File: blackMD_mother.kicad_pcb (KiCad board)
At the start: 2 copper layers, 99.1 x 99.1 mm, 19 parts

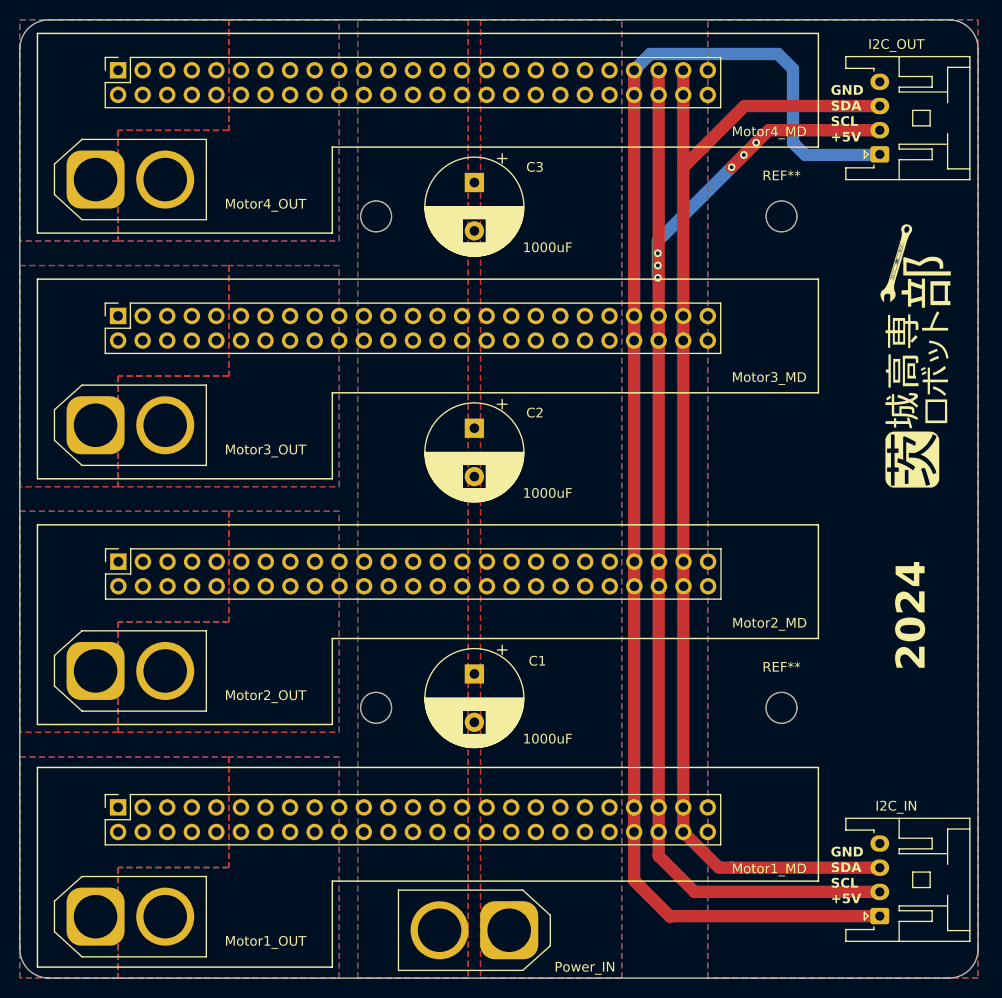
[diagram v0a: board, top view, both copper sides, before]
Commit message: swap MotorA & MotorB
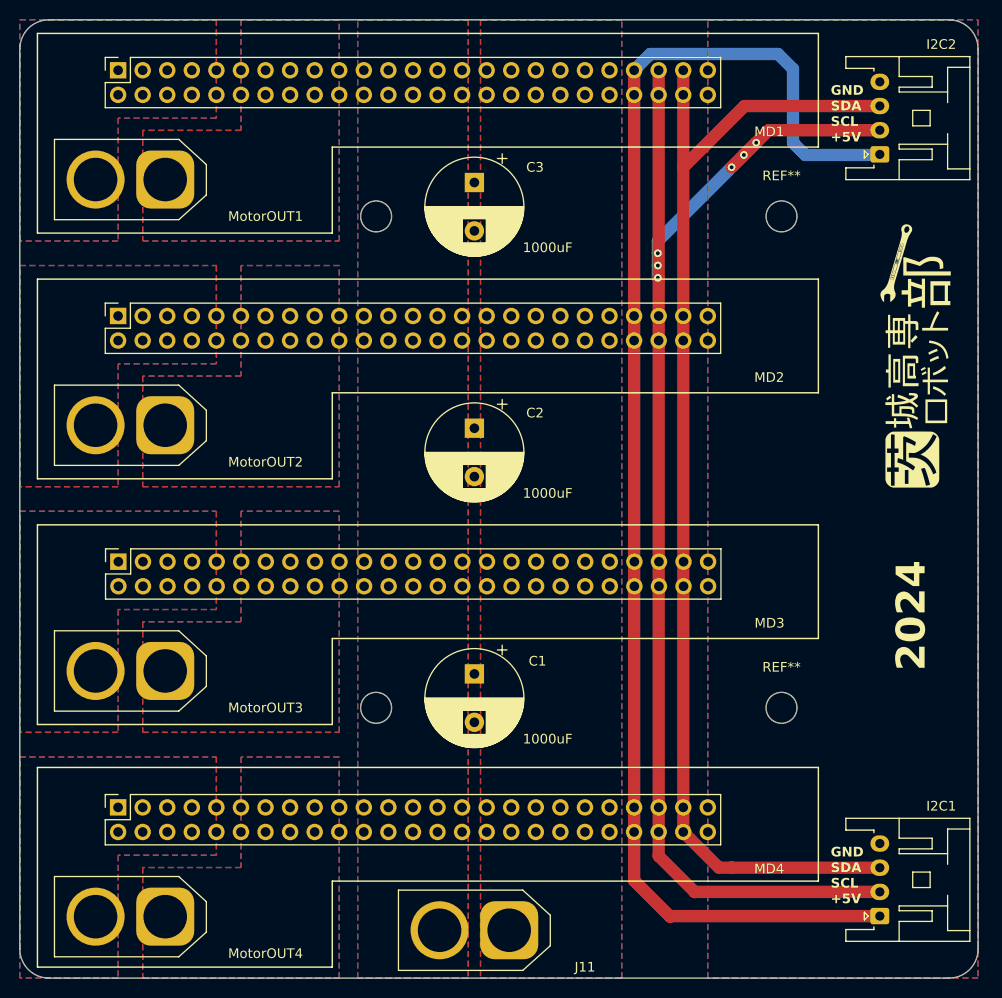
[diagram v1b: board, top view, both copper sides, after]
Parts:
- I2C1: renamed from I2C_IN; value I2C_IN -> S04B
- I2C2: renamed from I2C_OUT; value I2C_OUT -> S04B
- MD1: renamed from Motor4_MD; value MD_Socket1 -> XG4A-5071
- MD2: renamed from Motor3_MD; value MD_Socket2 -> XG4A-5071
- MD3: renamed from Motor2_MD; value MD_Socket3 -> XG4A-5071
- MD4: renamed from Motor1_MD; value MD_Socket4 -> XG4A-5071
- MotorOUT1: renamed from Motor4_OUT; value XT_Motor1 -> XT60
- MotorOUT2: renamed from Motor3_OUT; value XT_Motor2 -> XT60
- MotorOUT3: renamed from Motor2_OUT; value XT_Motor3 -> XT60
- MotorOUT4: renamed from Motor1_OUT; value XT_Motor4 -> XT60
- moved MotorOUT1 7.20 mm to (107.8, 71.1), turned to 180 degrees
- moved MotorOUT2 7.20 mm to (107.8, 96.5), turned to 180 degrees
- moved MotorOUT3 7.20 mm to (107.8, 121.9), turned to 180 degrees
- moved MotorOUT4 7.20 mm to (107.8, 147.3), turned to 180 degrees
- renumbered Power_IN to J11
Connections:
- MotorOUT1 pad 1: Motor_1A -> Motor_1B
- MotorOUT1 pad 2: Motor_1B -> Motor_1A
- MotorOUT2 pad 1: Motor_2A -> Motor_2B
- MotorOUT2 pad 2: Motor_2B -> Motor_2A
- MotorOUT3 pad 1: Motor_3A -> Motor_3B
- MotorOUT3 pad 2: Motor_3B -> Motor_3A
- MotorOUT4 pad 1: Motor_4A -> Motor_4B
- MotorOUT4 pad 2: Motor_4B -> Motor_4A

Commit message: add JLC
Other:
- board text added: "JLCJLCJLCJLC"
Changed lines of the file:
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@@
       (sketchpadsonfab false)
       (subtractmaskfromsilk false)
-      (outputformat 1)
+      (outputformat 4)
       (mirror false)
       (drillshape 0)
       (scaleselection 1)
-      (outputdirectory "gbrs/")
+      (outputdirectory "layers/")
     )
   )
@@
     (effects (font (size 1 1) (thickness 0.15)) (justify left bottom))
   )
+  (gr_text "JLCJLCJLCJLC" (at 191.851323 129.54 90) (layer "F.SilkS")
+    (effects (font (size 1 1) (thickness 0.15)) (justify left bottom))
+  )
   (dimension (type aligned) (layer "Dwgs.User")
     (pts (xy 92.791323 153.67) (xy 191.851323 153.67))
@@
   (segment (start 181.691323 142.26) (end 166.39 142.26) (width 1.27) (layer "F.Cu") (net 13))
   (segment (start 161.371323 69.85) (end 161.371323 59.824677) (width 1.27) (layer "F.Cu") (net 13))
-  (segment (start 167.64 68.58) (end 166.37 69.85) (width 1.27) (layer "F.Cu") (net 14))
+  (segment (start 163.911323 72.39) (end 170.281323 66.02) (width 1.27) (layer "F.Cu") (net 14))
   (segment (start 158.831323 59.824677) (end 158.831323 81.361323) (width 1.27) (layer "F.Cu") (net 14))
-  (segment (start 168.91 67.31) (end 167.64 68.58) (width 1.27) (layer "F.Cu") (net 14))
   (segment (start 158.831323 138.564677) (end 158.831323 141.051323) (width 1.27) (layer "F.Cu") (net 14))
   (segment (start 162.56 144.78) (end 162.58 144.76) (width 1.27) (layer "F.Cu") (net 14))
-  (segment (start 170.2 66.02) (end 168.91 67.31) (width 1.27) (layer "F.Cu") (net 14))
   (segment (start 158.831323 141.051323) (end 162.56 144.78) (width 1.27) (layer "F.Cu") (net 14))
   (segment (start 162.58 144.76) (end 181.691323 144.76) (width 1.27) (layer "F.Cu") (net 14))
-  (segment (start 181.691323 66.02) (end 170.2 66.02) (width 1.27) (layer "F.Cu") (net 14))
+  (segment (start 170.281323 66.02) (end 181.691323 66.02) (width 1.27) (layer "F.Cu") (net 14))
   (segment (start 158.831323 81.361323) (end 158.831323 138.564677) (width 1.27) (layer "F.Cu") (net 14))
-  (via (at 167.64 68.58) (size 0.8) (drill 0.4) (layers "F.Cu" "B.Cu") (net 14))
+  (via (at 163.911323 72.39) (size 0.8) (drill 0.4) (layers "F.Cu" "B.Cu") (net 14))
   (via (at 158.75 78.74) (size 0.8) (drill 0.4) (layers "F.Cu" "B.Cu") (net 14))
   (via (at 158.75 81.28) (size 0.8) (drill 0.4) (layers "F.Cu" "B.Cu") (net 14))
   (via (at 158.75 80.01) (size 0.8) (drill 0.4) (layers "F.Cu" "B.Cu") (net 14))
   (via (at 166.37 69.85) (size 0.8) (drill 0.4) (layers "F.Cu" "B.Cu") (net 14))
-  (via (at 168.91 67.31) (size 0.8) (drill 0.4) (layers "F.Cu" "B.Cu") (net 14))
+  (via (at 165.181323 71.12) (size 0.8) (drill 0.4) (layers "F.Cu" "B.Cu") (net 14))
   (segment (start 158.75 78.74) (end 158.75 80.01) (width 1.27) (layer "B.Cu") (net 14))
-  (segment (start 158.75 77.47) (end 168.91 67.31) (width 1.27) (layer "B.Cu") (net 14))
+  (segment (start 158.75 77.47) (end 166.37 69.85) (width 1.27) (layer "B.Cu") (net 14))
   (segment (start 158.75 80.01) (end 158.75 81.28) (width 1.27) (layer "B.Cu") (net 14))
   (segment (start 158.75 77.47) (end 158.75 78.74) (width 1.27) (layer "B.Cu") (net 14))
